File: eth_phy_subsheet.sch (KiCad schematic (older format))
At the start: 0 parts

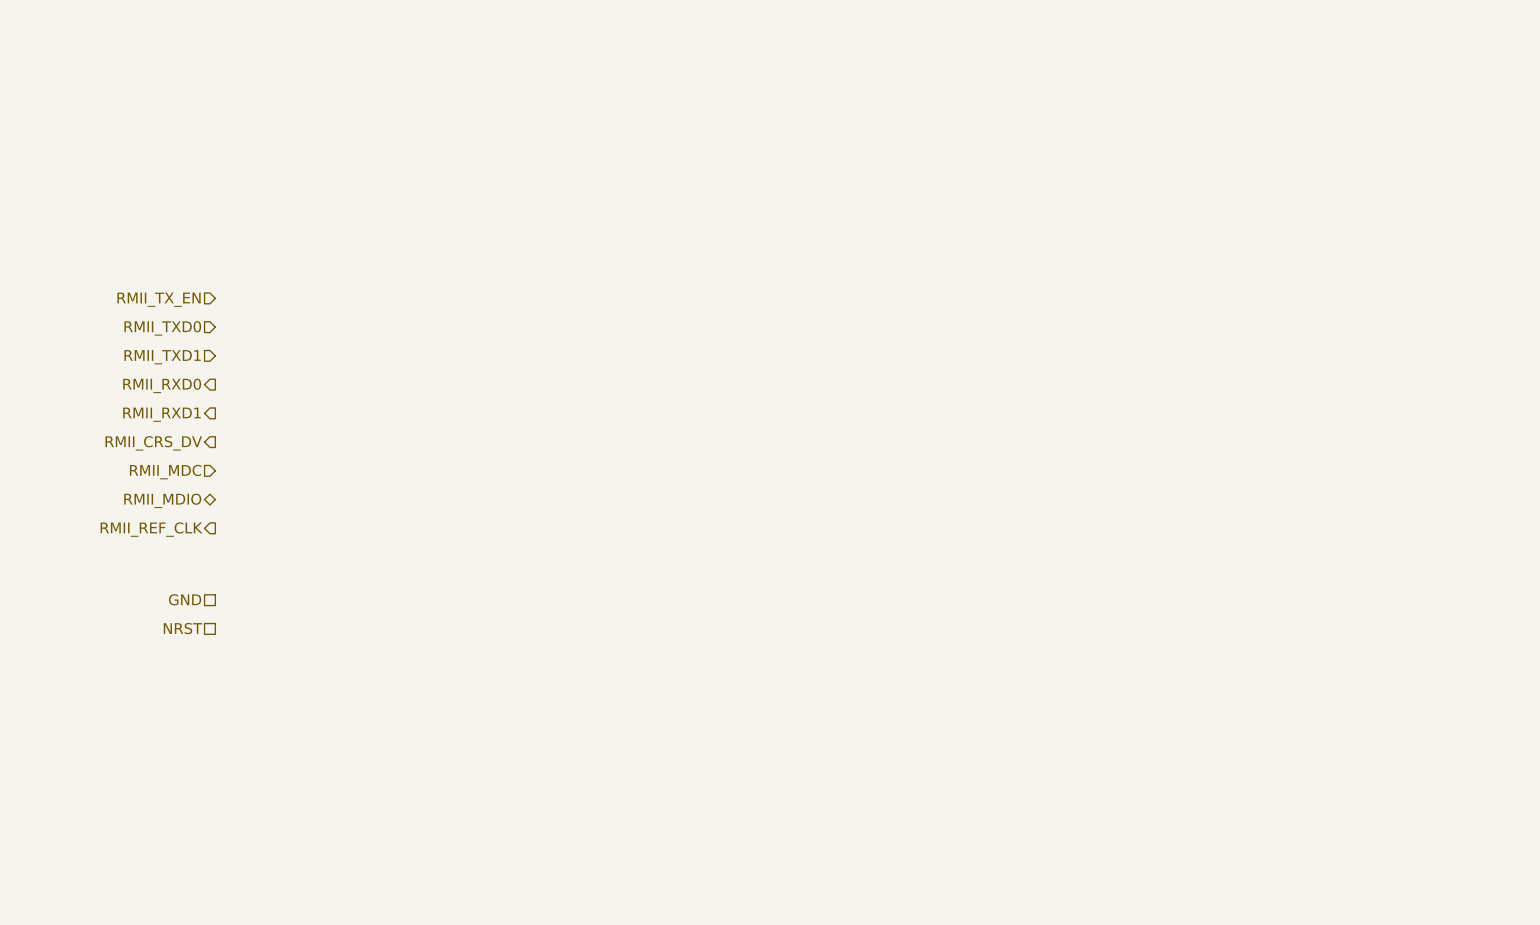
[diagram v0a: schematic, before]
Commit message: [Ethernet]: eth part update
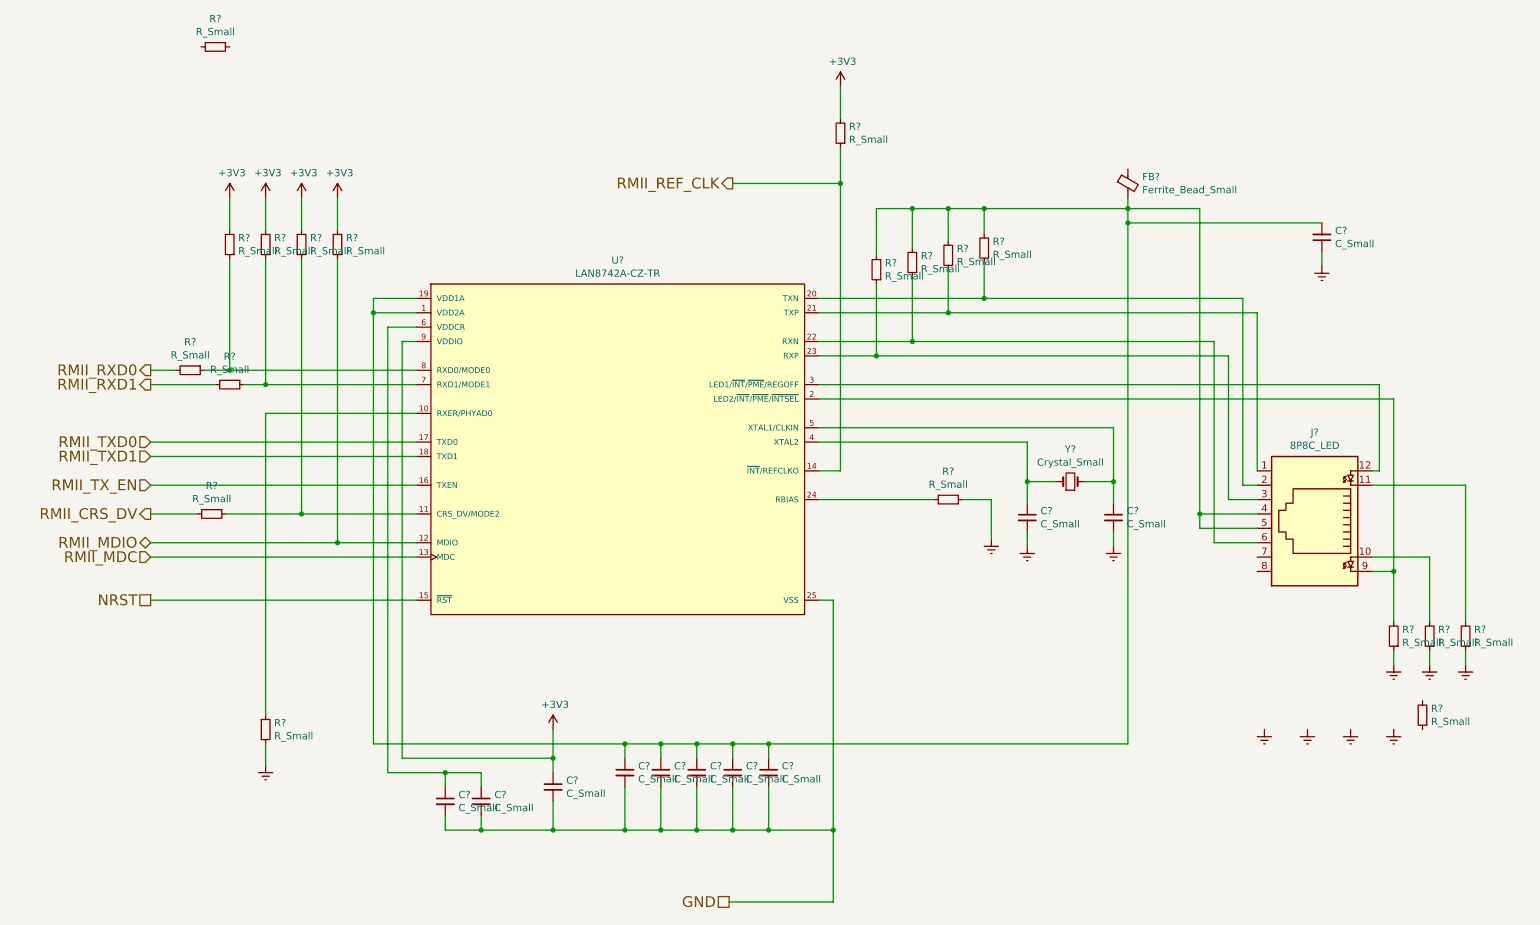
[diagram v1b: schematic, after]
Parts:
- added C? (x11): C_Small, symbol Device:C_Small
- added FB?: Ferrite_Bead_Small, symbol Device:Ferrite_Bead_Small
- added J?: 8P8C_LED, symbol Connector:8P8C_LED
- added R? (x19): R_Small, symbol Device:R_Small
- added U?: LAN8742A-CZ-TR, Microchip-C04-143B-S4QFN-0-0-*, symbol eec:LAN8742A-CZ-TR
- added Y?: Crystal_Small, Crystal:Crystal_SMD_Abracon_ABM3-2Pin_5.0x3.2mm_HandSoldering, symbol Device:Crystal_Small
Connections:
- net GND: now also C?.2, C?.2, C?.2, C?.2, C?.2, C?.2, C?.2, C?.2, U?.25 (VSS)
- net NRST: now also U?.15 (~RST~)
- net RMII_CRS_DV: now also R?.2
- net RMII_MDC: now also U?.13 (MDC)
- net RMII_MDIO: now also R?.1, U?.12 (MDIO)
- net RMII_REF_CLK: now also R?.1, U?.14 (~INT~/REFCLKO)
- net RMII_RXD0: now also R?.2
- net RMII_RXD1: now also R?.2
- net RMII_TXD0: now also U?.17 (TXD0)
- net RMII_TXD1: now also U?.18 (TXD1)
- net RMII_TX_EN: now also U?.16 (TXEN)
- new net: C?.1, C?.1, C?.1, C?.1, C?.1, C?.2, FB?.2, J?.4, J?.5, R?.2, R?.2, R?.2, R?.2, U?.1 (VDD2A), U?.19 (VDD1A)
- new net: R?.1, U?.10 (RXER/PHYAD0)
- new net: R?.1, R?.1, U?.11 (CRS_DV/MODE2)
- new net: J?.9, R?.2, U?.2 (LED2/~INT~/~PME~/~INTSEL~)
- new net: J?.2, R?.1, U?.20 (TXN)
- new net: J?.1, R?.1, U?.21 (TXP)
- new net: J?.6, R?.1, U?.22 (RXN)
- new net: J?.3, R?.1, U?.23 (RXP)
- new net: R?.2, U?.24 (RBIAS)
- new net: J?.12, U?.3 (LED1/~INT~/~PME~/REGOFF)
- new net: C?.1, U?.4 (XTAL2), Y?.1
- new net: C?.1, U?.5 (XTAL1/CLKIN), Y?.2
- new net: C?.1, C?.1, U?.6 (VDDCR)
- new net: R?.1, R?.1, U?.7 (RXD1/MODE1)
- new net: R?.1, R?.1, U?.8 (RXD0/MODE0)
- new net: J?.10, R?.2
- new net: J?.11, R?.2
- new net +3V3: C?.1, R?.2, R?.2, R?.2, R?.2, R?.2, U?.9 (VDDIO)
- new net Earth: C?.1, C?.2, C?.2, R?.1, R?.1, R?.1, R?.1, R?.2

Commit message: [Ethernet]: end schematic, but no nomenclature
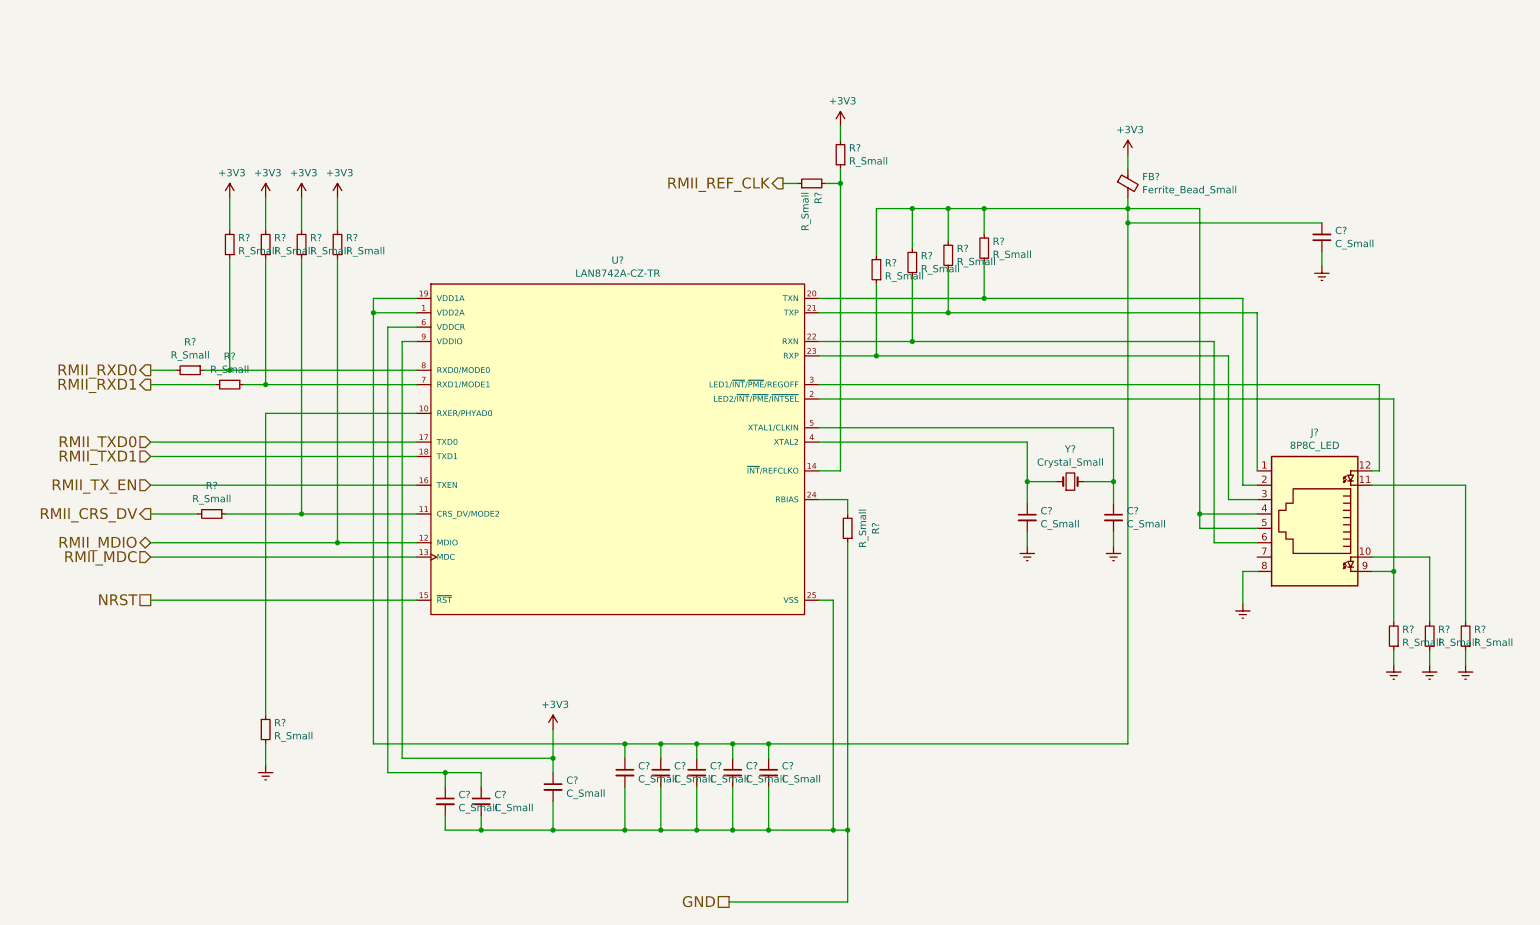
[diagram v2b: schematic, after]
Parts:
- removed R?: R_Small, symbol Device:R_Small
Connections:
- net +3V3: now also FB?.1
- net Earth: now also J?.8; no longer R?.1
- net GND: now also R?.1
- net RMII_REF_CLK: now also R?.1; no longer R?.1, U?.14 (~INT~/REFCLKO)
- net at R?.2: now also R?.1, U?.14 (~INT~/REFCLKO)
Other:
- moved on the sheet: R?
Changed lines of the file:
@@
 Text HLabel 1450 4500 0    75   BiDi ~ 0
 RMII_MDIO
-Text HLabel 5500 2000 0    75   Output ~ 0
+Text HLabel 5850 2000 0    75   Output ~ 0
 RMII_REF_CLK
 Text HLabel 5475 7000 0    75   UnSpc ~ 0
@@
 $Comp
 L Device:R_Small R?
-U 1 1 61C0B8A9
-P 1900 1050
-F 0 "R?" V 1704 1050 50  0000 C CNN
-F 1 "R_Small" V 1795 1050 50  0000 C CNN
-F 2 "" H 1900 1050 50  0001 C CNN
-F 3 "~" H 1900 1050 50  0001 C CNN
-	1    1900 1050
-	0    1    1    0
-$EndComp
-$Comp
-L Device:R_Small R?
 U 1 1 61C0BB62
 P 2000 2425
@@
 L Device:R_Small R?
 U 1 1 61C0CA6B
-P 6250 1650
-F 0 "R?" H 6191 1604 50  0000 R CNN
-F 1 "R_Small" H 6191 1695 50  0000 R CNN
-F 2 "" H 6250 1650 50  0001 C CNN
-F 3 "~" H 6250 1650 50  0001 C CNN
-	1    6250 1650
+P 6250 1800
+F 0 "R?" H 6191 1754 50  0000 R CNN
+F 1 "R_Small" H 6191 1845 50  0000 R CNN
+F 2 "" H 6250 1800 50  0001 C CNN
+F 3 "~" H 6250 1800 50  0001 C CNN
+	1    6250 1800
 	-1   0    0    1
 $EndComp
@@
 L Device:R_Small R?
 U 1 1 61C0CE21
-P 7000 4200
-F 0 "R?" V 6804 4200 50  0000 C CNN
-F 1 "R_Small" V 6895 4200 50  0000 C CNN
-F 2 "" H 7000 4200 50  0001 C CNN
-F 3 "~" H 7000 4200 50  0001 C CNN
-	1    7000 4200
-	0    1    1    0
+P 6300 4400
+F 0 "R?" V 6104 4400 50  0000 C CNN
+F 1 "R_Small" V 6195 4400 50  0000 C CNN
+F 2 "" H 6300 4400 50  0001 C CNN
+F 3 "~" H 6300 4400 50  0001 C CNN
+	1    6300 4400
+	-1   0    0    1
 $EndComp
 $Comp
@@
 L Device:R_Small R?
 U 1 1 61C107E8
-P 10300 5700
-F 0 "R?" H 10241 5654 50  0000 R CNN
-F 1 "R_Small" H 10241 5745 50  0000 R CNN
-F 2 "" H 10300 5700 50  0001 C CNN
-F 3 "~" H 10300 5700 50  0001 C CNN
-	1    10300 5700
-	-1   0    0    1
-$EndComp
-$Comp
-L power:Earth #PWR?
-U 1 1 61C10DE8
-P 10100 5800
-F 0 "#PWR?" H 10100 5550 50  0001 C CNN
-F 1 "Earth" H 10100 5650 50  0001 C CNN
-F 2 "" H 10100 5800 50  0001 C CNN
-F 3 "~" H 10100 5800 50  0001 C CNN
-	1    10100 5800
-	1    0    0    -1
-$EndComp
-$Comp
-L power:Earth #PWR?
-U 1 1 61C11E14
-P 9800 5800
-F 0 "#PWR?" H 9800 5550 50  0001 C CNN
-F 1 "Earth" H 9800 5650 50  0001 C CNN
-F 2 "" H 9800 5800 50  0001 C CNN
-F 3 "~" H 9800 5800 50  0001 C CNN
-	1    9800 5800
-	1    0    0    -1
-$EndComp
-$Comp
-L power:Earth #PWR?
-U 1 1 61C1208D
-P 9500 5800
-F 0 "#PWR?" H 9500 5550 50  0001 C CNN
-F 1 "Earth" H 9500 5650 50  0001 C CNN
-F 2 "" H 9500 5800 50  0001 C CNN
-F 3 "~" H 9500 5800 50  0001 C CNN
-	1    9500 5800
-	1    0    0    -1
+P 6050 2000
+F 0 "R?" H 5991 1954 50  0000 R CNN
+F 1 "R_Small" H 5991 2045 50  0000 R CNN
+F 2 "" H 6050 2000 50  0001 C CNN
+F 3 "~" H 6050 2000 50  0001 C CNN
+	1    6050 2000
+	0    -1   -1   0
 $EndComp
 $Comp
 L power:Earth #PWR?
 U 1 1 61C1233B
-P 9200 5800
-F 0 "#PWR?" H 9200 5550 50  0001 C CNN
-F 1 "Earth" H 9200 5650 50  0001 C CNN
-F 2 "" H 9200 5800 50  0001 C CNN
-F 3 "~" H 9200 5800 50  0001 C CNN
-	1    9200 5800
+P 9050 4925
+F 0 "#PWR?" H 9050 4675 50  0001 C CNN
+F 1 "Earth" H 9050 4775 50  0001 C CNN
+F 2 "" H 9050 4925 50  0001 C CNN
+F 3 "~" H 9050 4925 50  0001 C CNN
+	1    9050 4925
 	1    0    0    -1
 $EndComp
@@
 Wire Wire Line
 	6100 3800 7550 3800
-$Comp
-L power:Earth #PWR?
-U 1 1 61C97C7D
-P 7300 4475
-F 0 "#PWR?" H 7300 4225 50  0001 C CNN
-F 1 "Earth" H 7300 4325 50  0001 C CNN
-F 2 "" H 7300 4475 50  0001 C CNN
-F 3 "~" H 7300 4475 50  0001 C CNN
-	1    7300 4475
-	1    0    0    -1
-$EndComp
-Wire Wire Line
-	7100 4200 7300 4200
-Wire Wire Line
-	7300 4200 7300 4475
 Connection ~ 8250 2175
 Wire Wire Line
@@
 L power:+3V3 #PWR?
 U 1 1 61D32C24
-P 6250 1325
-F 0 "#PWR?" H 6250 1175 50  0001 C CNN
-F 1 "+3V3" H 6265 1498 50  0000 C CNN
-F 2 "" H 6250 1325 50  0001 C CNN
-F 3 "" H 6250 1325 50  0001 C CNN
-	1    6250 1325
+P 6250 1600
+F 0 "#PWR?" H 6250 1450 50  0001 C CNN
+F 1 "+3V3" H 6265 1773 50  0000 C CNN
+F 2 "" H 6250 1600 50  0001 C CNN
+F 3 "" H 6250 1600 50  0001 C CNN
+	1    6250 1600
 	1    0    0    -1
 $EndComp
@@
 Wire Wire Line
 	2750 2100 2750 2325
-Wire Wire Line
-	6250 1325 6250 1550
 Wire Wire Line
 	1825 3300 2000 3300
@@
 Wire Wire Line
 	6200 4900 6200 6500
-Wire Wire Line
-	6200 7000 5475 7000
 $Comp
 L Device:C_Small C?
@@
 	4250 6500 4750 6500
 Connection ~ 4250 6500
-Connection ~ 6200 6500
-Wire Wire Line
-	6200 6500 6200 7000
 Wire Wire Line
 	5750 6200 5750 6500
@@
 	7550 4075 7750 4075
 Connection ~ 8150 4075
-Wire Wire Line
-	6100 4200 6900 4200
 Wire Wire Line
 	8250 2275 8250 5900
@@
 	6100 2800 7250 2800
 Wire Wire Line
-	5500 2000 6250 2000
-Wire Wire Line
-	6250 2000 6250 1750
+	6250 2000 6250 1900
 Wire Wire Line
 	6250 2000 6250 4000
@@
 Wire Wire Line
 	2250 3600 3300 3600
+Wire Wire Line
+	9150 4700 9050 4700
+Wire Wire Line
+	9050 4700 9050 4925
+$Comp
+L power:+3V3 #PWR?
+U 1 1 61CE0856
+P 8250 1800
+F 0 "#PWR?" H 8250 1650 50  0001 C CNN
+F 1 "+3V3" H 8265 1973 50  0000 C CNN
+F 2 "" H 8250 1800 50  0001 C CNN
+F 3 "" H 8250 1800 50  0001 C CNN
+	1    8250 1800
+	1    0    0    -1
+$EndComp
+Wire Wire Line
+	8250 1800 8250 1900
+Wire Wire Line
+	6200 6500 6300 6500
+Wire Wire Line
+	6300 6500 6300 4500
+Wire Wire Line
+	6300 4200 6100 4200
+Connection ~ 6200 6500
+Wire Wire Line
+	6300 4300 6300 4200
+Wire Wire Line
+	6300 6500 6300 7000
+Wire Wire Line
+	5475 7000 6300 7000
+Connection ~ 6300 6500
+Wire Wire Line
+	6150 2000 6250 2000
+Wire Wire Line
+	6250 1600 6250 1700
+Wire Wire Line
+	5950 2000 5850 2000
 $EndSCHEMATC

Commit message: [MCU]: mcu update
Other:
- moved on the sheet: C?, Y?
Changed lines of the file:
@@
 $EndComp
-$Comp
-L Device:Crystal_Small Y?
-U 1 1 61BFFA80
-P 7850 4075
-F 0 "Y?" H 7850 4300 50  0000 C CNN
-F 1 "Crystal_Small" H 7850 4209 50  0000 C CNN
-F 2 "Crystal:Crystal_SMD_Abracon_ABM3-2Pin_5.0x3.2mm_HandSoldering" H 7850 4075 50  0001 C CNN
-F 3 "~" H 7850 4075 50  0001 C CNN
-	1    7850 4075
-	1    0    0    -1
-$EndComp
-Wire Wire Line
-	7950 4075 8150 4075
-$Comp
-L Device:C_Small C?
-U 1 1 61C02B58
-P 7550 4325
-F 0 "C?" H 7642 4371 50  0000 L CNN
-F 1 "C_Small" H 7642 4280 50  0000 L CNN
-F 2 "" H 7550 4325 50  0001 C CNN
-F 3 "~" H 7550 4325 50  0001 C CNN
-	1    7550 4325
-	1    0    0    -1
-$EndComp
-$Comp
-L Device:C_Small C?
-U 1 1 61C02FC7
-P 8150 4325
-F 0 "C?" H 8242 4371 50  0000 L CNN
-F 1 "C_Small" H 8242 4280 50  0000 L CNN
-F 2 "" H 8150 4325 50  0001 C CNN
-F 3 "~" H 8150 4325 50  0001 C CNN
-	1    8150 4325
-	1    0    0    -1
-$EndComp
-$Comp
-L power:Earth #PWR?
-U 1 1 61C043D9
-P 7550 4525
-F 0 "#PWR?" H 7550 4275 50  0001 C CNN
-F 1 "Earth" H 7550 4375 50  0001 C CNN
-F 2 "" H 7550 4525 50  0001 C CNN
-F 3 "~" H 7550 4525 50  0001 C CNN
-	1    7550 4525
-	1    0    0    -1
-$EndComp
-$Comp
-L power:Earth #PWR?
-U 1 1 61C04801
-P 8150 4525
-F 0 "#PWR?" H 8150 4275 50  0001 C CNN
-F 1 "Earth" H 8150 4375 50  0001 C CNN
-F 2 "" H 8150 4525 50  0001 C CNN
-F 3 "~" H 8150 4525 50  0001 C CNN
-	1    8150 4525
-	1    0    0    -1
-$EndComp
-Wire Wire Line
-	7550 4225 7550 4075
-Wire Wire Line
-	8150 4225 8150 4075
-Wire Wire Line
-	8150 4425 8150 4525
-Wire Wire Line
-	7550 4525 7550 4425
 $Comp
 L power:Earth #PWR?
@@
 Wire Wire Line
 	10100 4700 10100 5050
-Wire Wire Line
-	6100 3500 10100 3500
 Connection ~ 10100 4700
 Wire Wire Line
 	10100 3500 10100 4700
-Wire Wire Line
-	6100 3400 10000 3400
 Wire Wire Line
 	10000 3400 10000 4000
@@
 	8750 4400 8750 4300
 Connection ~ 8750 4300
-Wire Wire Line
-	6100 3700 8150 3700
-Wire Wire Line
-	6100 3800 7550 3800
 Connection ~ 8250 2175
 Wire Wire Line
@@
 	9600 2275 8250 2275
 Wire Wire Line
-	7550 3800 7550 4075
-Connection ~ 7550 4075
-Wire Wire Line
-	8150 3700 8150 4075
-Wire Wire Line
-	7550 4075 7750 4075
-Connection ~ 8150 4075
-Wire Wire Line
 	8250 2275 8250 5900
 Wire Wire Line
@@
 Connection ~ 6500 3200
 Wire Wire Line
-	6500 3200 8950 3200
-Wire Wire Line
 	6500 2175 6750 2175
 Wire Wire Line
 	6750 2450 6750 2175
-Wire Wire Line
-	6750 2650 6750 3100
 $Comp
 L Device:R_Small R?
@@
 Wire Wire Line
 	5950 2000 5850 2000
+Wire Wire Line
+	6750 2650 6750 3100
+Wire Wire Line
+	6100 3500 10100 3500
+Wire Wire Line
+	6100 3400 10000 3400
+Wire Wire Line
+	6500 3200 8950 3200
+$Comp
+L Device:Crystal_Small Y?
+U 1 1 61BFFA80
+P 7025 4075
+F 0 "Y?" H 7025 4300 50  0000 C CNN
+F 1 "Crystal_Small" H 7025 4209 50  0000 C CNN
+F 2 "Crystal:Crystal_SMD_Abracon_ABM3-2Pin_5.0x3.2mm_HandSoldering" H 7025 4075 50  0001 C CNN
+F 3 "~" H 7025 4075 50  0001 C CNN
+	1    7025 4075
+	1    0    0    -1
+$EndComp
+Wire Wire Line
+	7125 4075 7325 4075
+$Comp
+L Device:C_Small C?
+U 1 1 61C02B58
+P 6725 4325
+F 0 "C?" H 6817 4371 50  0000 L CNN
+F 1 "C_Small" H 6817 4280 50  0000 L CNN
+F 2 "" H 6725 4325 50  0001 C CNN
+F 3 "~" H 6725 4325 50  0001 C CNN
+	1    6725 4325
+	1    0    0    -1
+$EndComp
+$Comp
+L Device:C_Small C?
+U 1 1 61C02FC7
+P 7325 4325
+F 0 "C?" H 7417 4371 50  0000 L CNN
+F 1 "C_Small" H 7417 4280 50  0000 L CNN
+F 2 "" H 7325 4325 50  0001 C CNN
+F 3 "~" H 7325 4325 50  0001 C CNN
+	1    7325 4325
+	1    0    0    -1
+$EndComp
+$Comp
+L power:Earth #PWR?
+U 1 1 61C043D9
+P 6725 4525
+F 0 "#PWR?" H 6725 4275 50  0001 C CNN
+F 1 "Earth" H 6725 4375 50  0001 C CNN
+F 2 "" H 6725 4525 50  0001 C CNN
+F 3 "~" H 6725 4525 50  0001 C CNN
+	1    6725 4525
+	1    0    0    -1
+$EndComp
+$Comp
+L power:Earth #PWR?
+U 1 1 61C04801
+P 7325 4525
+F 0 "#PWR?" H 7325 4275 50  0001 C CNN
+F 1 "Earth" H 7325 4375 50  0001 C CNN
+F 2 "" H 7325 4525 50  0001 C CNN
+F 3 "~" H 7325 4525 50  0001 C CNN
+	1    7325 4525
+	1    0    0    -1
+$EndComp
+Wire Wire Line
+	6725 4225 6725 4075
+Wire Wire Line
+	7325 4225 7325 4075
+Wire Wire Line
+	7325 4425 7325 4525
+Wire Wire Line
+	6725 4525 6725 4425
+Wire Wire Line
+	6725 3800 6725 4075
+Connection ~ 6725 4075
+Wire Wire Line
+	7325 3700 7325 4075
+Wire Wire Line
+	6725 4075 6925 4075
+Connection ~ 7325 4075
+Wire Wire Line
+	6100 3700 7325 3700
+Wire Wire Line
+	6100 3800 6725 3800
 $EndSCHEMATC
